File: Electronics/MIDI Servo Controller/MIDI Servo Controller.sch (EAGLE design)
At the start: 26 parts, among them Q1 20MHz, T1 2N3904, X1 SIGNAL-PWR-GND, X2 SIGNAL-PWR-GND

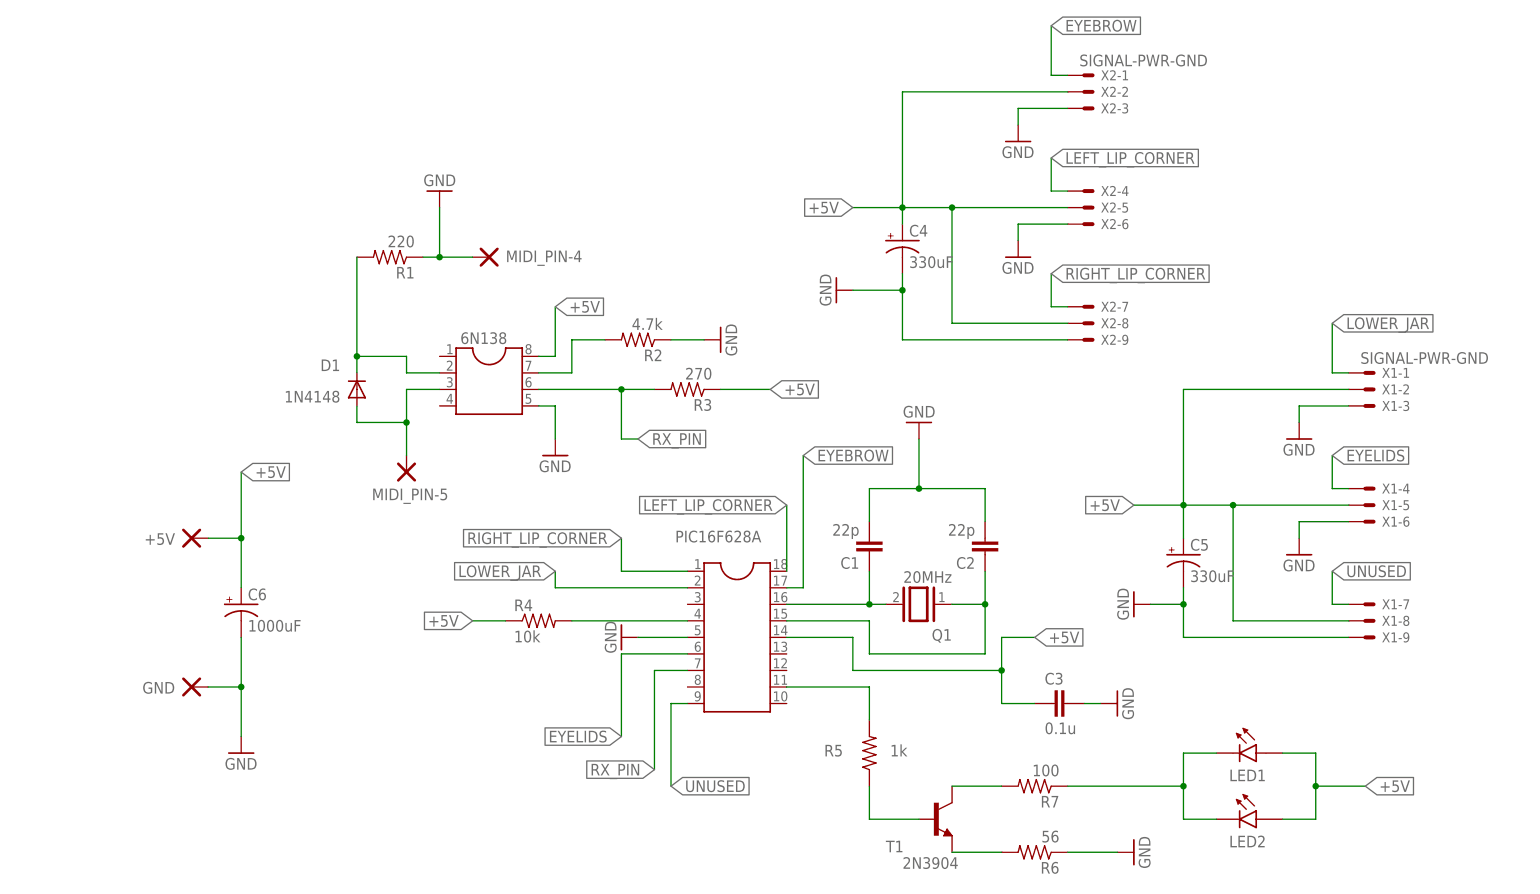
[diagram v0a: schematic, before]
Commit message: Cleaned up schematic and board layout.
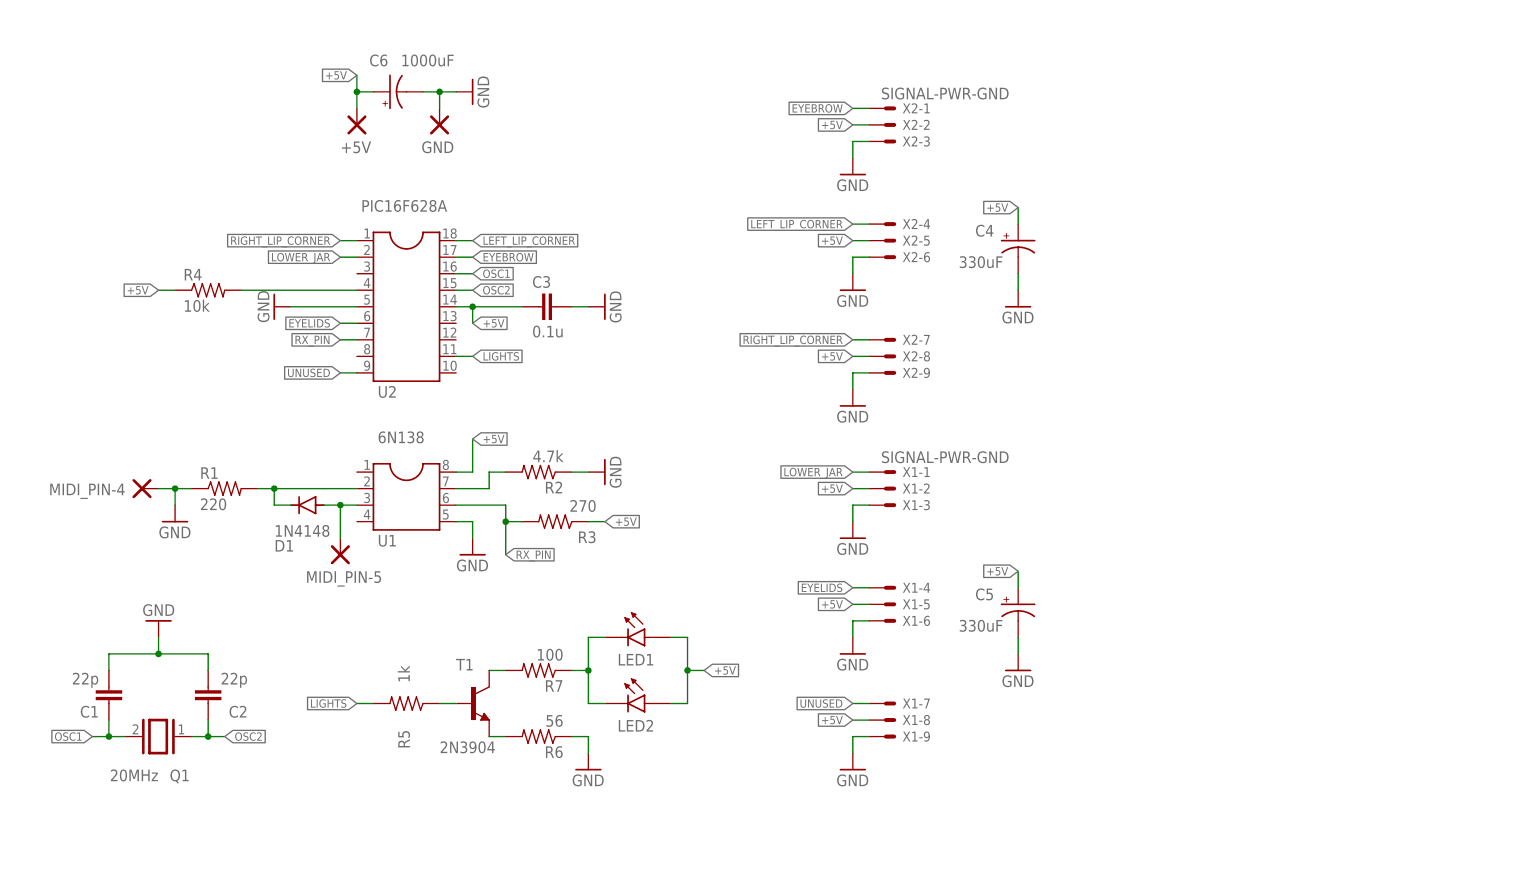
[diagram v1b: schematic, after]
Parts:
- 6N138: value (none) -> U1
- PIC16F628A: value (none) -> U2
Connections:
- net N$3 renamed OSC1
- net N$4 renamed OSC2
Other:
- moved on the sheet: +5V, 6N138, C1, C2, C3, C4, C5, C6, GND, LED1, LED2, MIDI_PIN-4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

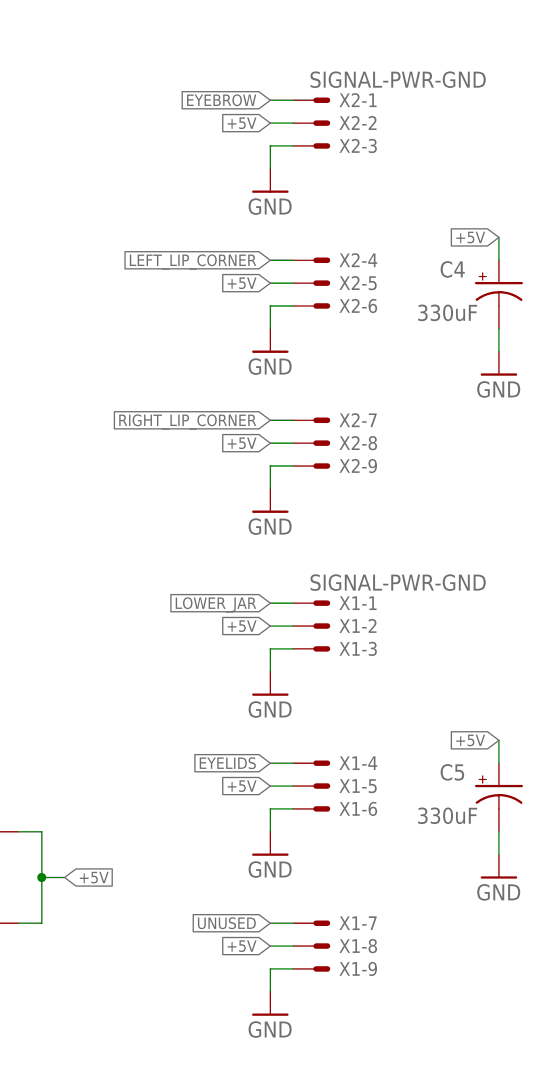
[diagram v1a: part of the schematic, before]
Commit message: Updated schematic and board layout with updated component library.
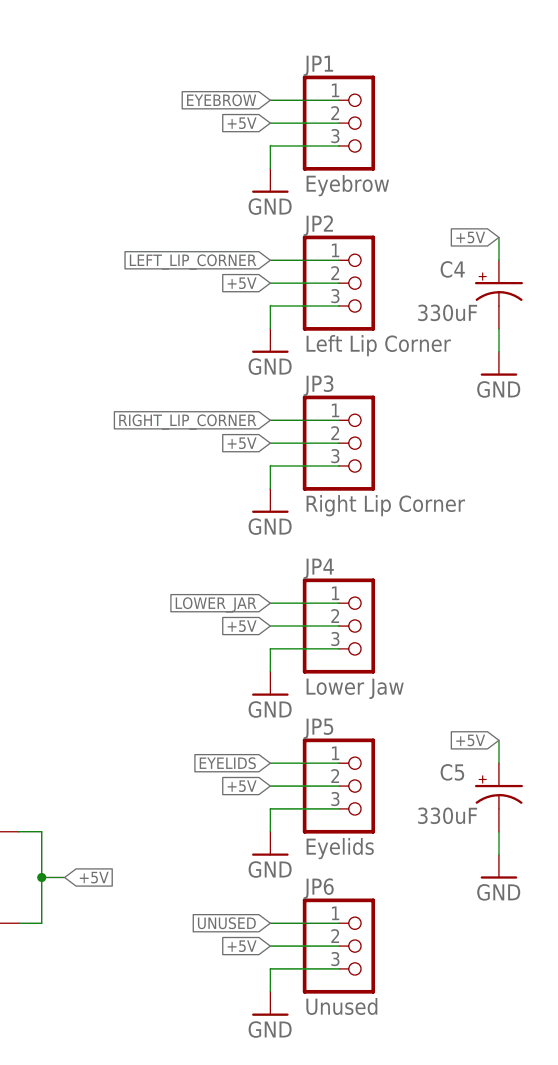
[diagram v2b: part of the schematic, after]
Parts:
- removed X1, X2: SIGNAL-PWR-GND, con-molex:22-23-2091
- added JP1: Eyebrow, adafruit:PINHD-1X3
- added JP2: Left Lip Corner, adafruit:PINHD-1X3
- added JP3: Right Lip Corner, adafruit:PINHD-1X3
- added JP4: Lower Jaw, adafruit:PINHD-1X3
- added JP5: Eyelids, adafruit:PINHD-1X3
- added JP6: Unused, adafruit:PINHD-1X3
- +5V, GND, MIDI_PIN-4, MIDI_PIN-5: device DOUBLE_THROUGH_HOLE_PAD:DOUBLE_THROUGH_HOLE_PAD -> Double-Through-Hole-Pad:DOUBLE_THROUGH_HOLE_PAD
- LED1, LED2: device REMOTE_LED:REMOTE_LED -> Remote-LED:REMOTE_LED
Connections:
- net +5V: now also JP1.2, JP2.2, JP3.2, JP4.2, JP5.2, JP6.2; no longer X1-2.S, X1-5.S, X1-8.S, X2-2.S, X2-5.S, X2-8.S
- net EYEBROW: now also JP1.1; no longer X2-1.S
- net EYELIDS: now also JP5.1; no longer X1-4.S
- net GND: now also JP1.3, JP2.3, JP3.3, JP4.3, JP5.3, JP6.3; no longer X1-3.S, X1-6.S, X1-9.S, X2-3.S, X2-6.S, X2-9.S
- net LEFT_LIP_CORNER: now also JP2.1; no longer X2-4.S
- net LOWER_JAR: now also JP4.1; no longer X1-1.S
- net RIGHT_LIP_CORNER: now also JP3.1; no longer X2-7.S
- net UNUSED: now also JP6.1; no longer X1-7.S
